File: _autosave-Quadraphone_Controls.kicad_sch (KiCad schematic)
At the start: 16 parts, among them SW1 SYNCH_SWITCH, SW2 DPDT_Switch

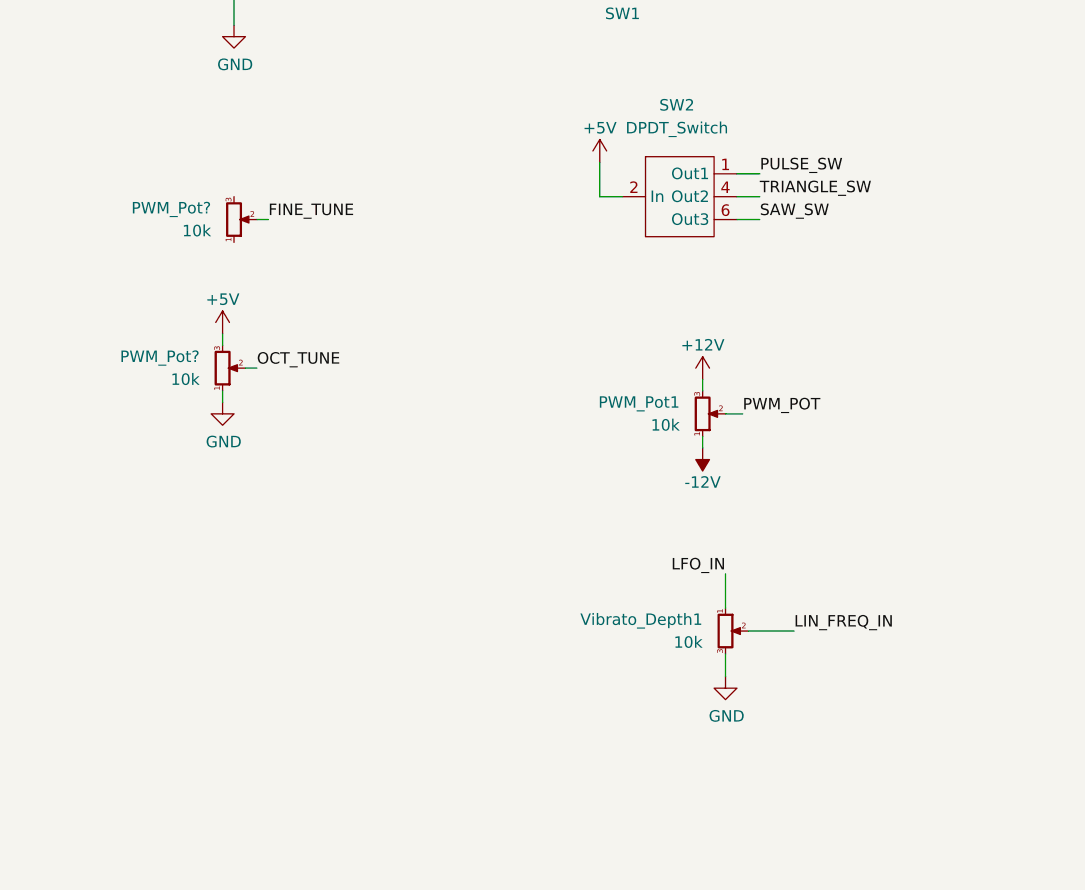
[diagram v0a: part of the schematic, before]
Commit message: Started control board schematic
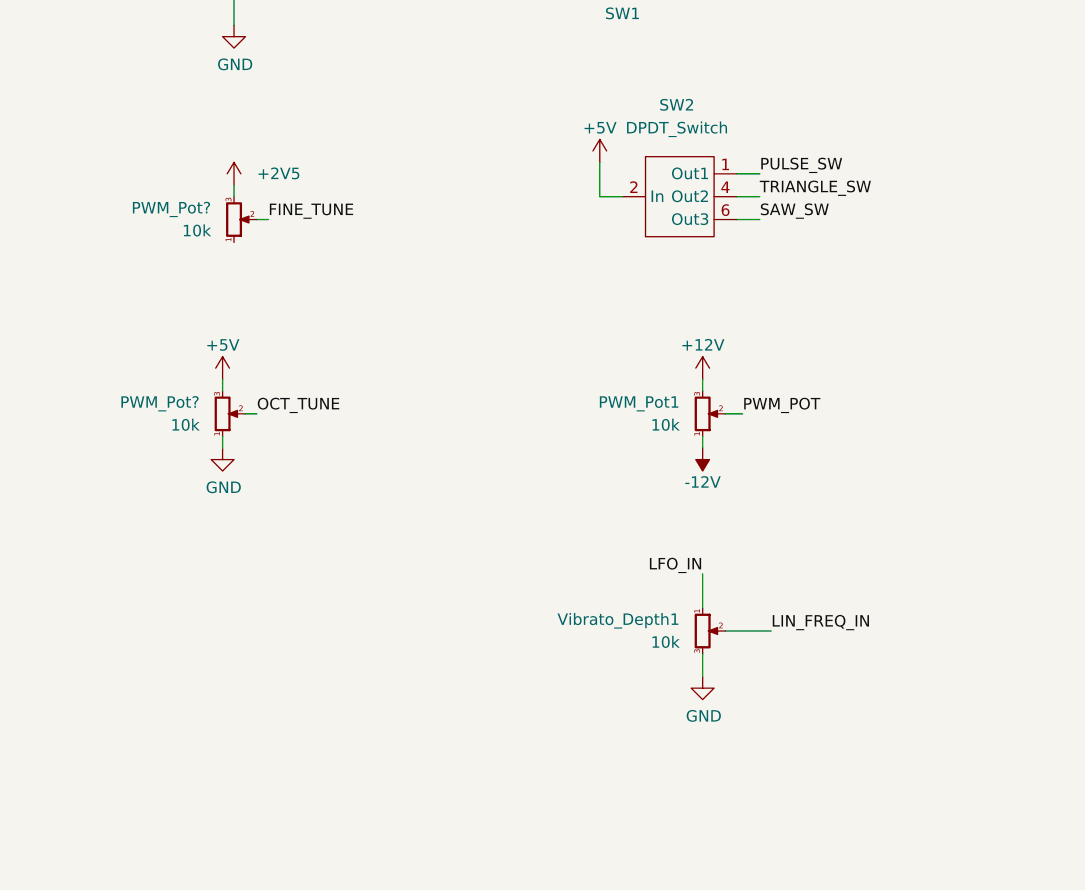
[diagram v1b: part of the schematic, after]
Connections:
- net +2V5: now also PWM_Pot?.3
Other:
- moved on the sheet: PWM_Pot?, Vibrato_Depth1
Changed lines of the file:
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@@
     (stroke (width 0) (type default) (color 0 0 0 0))
   )
-  (wire (pts (xy 36.83 95.25) (xy 36.83 93.98))
+  (wire (pts (xy 36.83 100.33) (xy 36.83 99.06))
     (stroke (width 0) (type default) (color 0 0 0 0))
   )
@@
     (stroke (width 0) (type default) (color 0 0 0 0))
   )
-  (wire (pts (xy 36.83 87.63) (xy 36.83 88.9))
-    (stroke (width 0) (type default) (color 0 0 0 0))
-  )
-  (wire (pts (xy 92.71 123.19) (xy 92.71 125.73))
+  (wire (pts (xy 36.83 92.71) (xy 36.83 93.98))
+    (stroke (width 0) (type default) (color 0 0 0 0))
+  )
+  (wire (pts (xy 90.17 123.19) (xy 90.17 125.73))
     (stroke (width 0) (type default) (color 0 0 0 0))
   )
@@
     (stroke (width 0) (type default) (color 0 0 0 0))
   )
-  (wire (pts (xy 95.25 120.65) (xy 100.33 120.65))
+  (wire (pts (xy 92.71 120.65) (xy 97.79 120.65))
     (stroke (width 0) (type default) (color 0 0 0 0))
   )
@@
     (stroke (width 0) (type default) (color 0 0 0 0))
   )
-  (wire (pts (xy 39.37 91.44) (xy 40.64 91.44))
+  (wire (pts (xy 39.37 96.52) (xy 40.64 96.52))
     (stroke (width 0) (type default) (color 0 0 0 0))
   )
@@
     (stroke (width 0) (type default) (color 0 0 0 0))
   )
-  (wire (pts (xy 92.71 114.3) (xy 92.71 118.11))
+  (wire (pts (xy 90.17 114.3) (xy 90.17 118.11))
     (stroke (width 0) (type default) (color 0 0 0 0))
   )
@@
     (stroke (width 0) (type default) (color 0 0 0 0))
   )
+  (wire (pts (xy 38.1 71.12) (xy 38.1 72.39))
+    (stroke (width 0) (type default) (color 0 0 0 0))
+  )
   (wire (pts (xy 74.93 46.99) (xy 77.47 46.99))
     (stroke (width 0) (type default) (color 0 0 0 0))
@@
     (effects (font (size 1.27 1.27)) (justify left bottom))
   )
-  (label "LFO_IN" (at 92.71 114.3 180)
+  (label "LFO_IN" (at 90.17 114.3 180)
     (effects (font (size 1.27 1.27)) (justify right bottom))
   )
@@
     (effects (font (size 1.27 1.27)) (justify left bottom))
   )
-  (label "LIN_FREQ_IN" (at 100.33 120.65 0)
+  (label "LIN_FREQ_IN" (at 97.79 120.65 0)
     (effects (font (size 1.27 1.27)) (justify left bottom))
   )
@@
     (effects (font (size 1.27 1.27)) (justify left bottom))
   )
-  (label "OCT_TUNE" (at 40.64 91.44 0)
+  (label "OCT_TUNE" (at 40.64 96.52 0)
     (effects (font (size 1.27 1.27)) (justify left bottom))
   )
@@
     (pin "1")
   )
-  (symbol (lib_id "Device:R_Potentiometer_Small") (at 36.83 91.44 0) (mirror x) (unit 1)
-    (in_bom yes) (on_board yes) (fields_autoplaced)
-    (property "Reference" "PWM_Pot?" (id 0) (at 34.29 90.1699 0)
-      (effects (font (size 1.27 1.27)) (justify right))
-    )
-    (property "Value" "10k" (id 1) (at 34.29 92.7099 0)
-      (effects (font (size 1.27 1.27)) (justify right))
-    )
-    (property "Footprint" "Custom_Footprints:Alpha_9mm_Potentiometer_Aligned" (id 2) (at 36.83 91.44 0)
-      (effects (font (size 1.27 1.27)) hide)
-    )
-    (property "Datasheet" "~" (id 3) (at 36.83 91.44 0)
+  (symbol (lib_id "Device:R_Potentiometer_Small") (at 36.83 96.52 0) (mirror x) (unit 1)
+    (in_bom yes) (on_board yes) (fields_autoplaced)
+    (property "Reference" "PWM_Pot?" (id 0) (at 34.29 95.2499 0)
+      (effects (font (size 1.27 1.27)) (justify right))
+    )
+    (property "Value" "10k" (id 1) (at 34.29 97.7899 0)
+      (effects (font (size 1.27 1.27)) (justify right))
+    )
+    (property "Footprint" "Custom_Footprints:Alpha_9mm_Potentiometer_Aligned" (id 2) (at 36.83 96.52 0)
+      (effects (font (size 1.27 1.27)) hide)
+    )
+    (property "Datasheet" "~" (id 3) (at 36.83 96.52 0)
       (effects (font (size 1.27 1.27)) hide)
     )
@@
     (pin "8")
   )
-  (symbol (lib_id "Device:R_Potentiometer_Small") (at 92.71 120.65 0) (unit 1)
-    (in_bom yes) (on_board yes) (fields_autoplaced)
-    (property "Reference" "Vibrato_Depth1" (id 0) (at 90.17 119.3799 0)
-      (effects (font (size 1.27 1.27)) (justify right))
-    )
-    (property "Value" "10k" (id 1) (at 90.17 121.9199 0)
-      (effects (font (size 1.27 1.27)) (justify right))
-    )
-    (property "Footprint" "Custom_Footprints:Alpha_9mm_Potentiometer_Aligned" (id 2) (at 92.71 120.65 0)
-      (effects (font (size 1.27 1.27)) hide)
-    )
-    (property "Datasheet" "~" (id 3) (at 92.71 120.65 0)
+  (symbol (lib_id "Device:R_Potentiometer_Small") (at 90.17 120.65 0) (unit 1)
+    (in_bom yes) (on_board yes) (fields_autoplaced)
+    (property "Reference" "Vibrato_Depth1" (id 0) (at 87.63 119.3799 0)
+      (effects (font (size 1.27 1.27)) (justify right))
+    )
+    (property "Value" "10k" (id 1) (at 87.63 121.9199 0)
+      (effects (font (size 1.27 1.27)) (justify right))
+    )
+    (property "Footprint" "Custom_Footprints:Alpha_9mm_Potentiometer_Aligned" (id 2) (at 90.17 120.65 0)
+      (effects (font (size 1.27 1.27)) hide)
+    )
+    (property "Datasheet" "~" (id 3) (at 90.17 120.65 0)
       (effects (font (size 1.27 1.27)) hide)
     )
@@
     (pin "1")
   )
-  (symbol (lib_id "power:GND") (at 36.83 95.25 0) (unit 1)
-    (in_bom yes) (on_board yes)
-    (property "Reference" "#PWR?" (id 0) (at 36.83 101.6 0)
-      (effects (font (size 1.27 1.27)) hide)
-    )
-    (property "Value" "GND" (id 1) (at 36.957 99.6442 0))
-    (property "Footprint" "" (id 2) (at 36.83 95.25 0)
-      (effects (font (size 1.27 1.27)) hide)
-    )
-    (property "Datasheet" "" (id 3) (at 36.83 95.25 0)
+  (symbol (lib_id "power:GND") (at 36.83 100.33 0) (unit 1)
+    (in_bom yes) (on_board yes)
+    (property "Reference" "#PWR?" (id 0) (at 36.83 106.68 0)
+      (effects (font (size 1.27 1.27)) hide)
+    )
+    (property "Value" "GND" (id 1) (at 36.957 104.7242 0))
+    (property "Footprint" "" (id 2) (at 36.83 100.33 0)
+      (effects (font (size 1.27 1.27)) hide)
+    )
+    (property "Datasheet" "" (id 3) (at 36.83 100.33 0)
       (effects (font (size 1.27 1.27)) hide)
     )
@@
     (pin "9")
   )
-  (symbol (lib_id "power:GND") (at 92.71 125.73 0) (unit 1)
-    (in_bom yes) (on_board yes)
-    (property "Reference" "#PWR023" (id 0) (at 92.71 132.08 0)
-      (effects (font (size 1.27 1.27)) hide)
-    )
-    (property "Value" "GND" (id 1) (at 92.837 130.1242 0))
-    (property "Footprint" "" (id 2) (at 92.71 125.73 0)
-      (effects (font (size 1.27 1.27)) hide)
-    )
-    (property "Datasheet" "" (id 3) (at 92.71 125.73 0)
-      (effects (font (size 1.27 1.27)) hide)
-    )
-    (pin "1")
-  )
-  (symbol (lib_id "power:+5V") (at 36.83 87.63 0) (unit 1)
-    (in_bom yes) (on_board yes)
-    (property "Reference" "#PWR?" (id 0) (at 36.83 91.44 0)
-      (effects (font (size 1.27 1.27)) hide)
-    )
-    (property "Value" "+5V" (id 1) (at 36.83 83.82 0))
-    (property "Footprint" "" (id 2) (at 36.83 87.63 0)
-      (effects (font (size 1.27 1.27)) hide)
-    )
-    (property "Datasheet" "" (id 3) (at 36.83 87.63 0)
+  (symbol (lib_id "power:GND") (at 90.17 125.73 0) (unit 1)
+    (in_bom yes) (on_board yes)
+    (property "Reference" "#PWR023" (id 0) (at 90.17 132.08 0)
+      (effects (font (size 1.27 1.27)) hide)
+    )
+    (property "Value" "GND" (id 1) (at 90.297 130.1242 0))
+    (property "Footprint" "" (id 2) (at 90.17 125.73 0)
+      (effects (font (size 1.27 1.27)) hide)
+    )
+    (property "Datasheet" "" (id 3) (at 90.17 125.73 0)
+      (effects (font (size 1.27 1.27)) hide)
+    )
+    (pin "1")
+  )
+  (symbol (lib_id "power:+5V") (at 36.83 92.71 0) (unit 1)
+    (in_bom yes) (on_board yes)
+    (property "Reference" "#PWR?" (id 0) (at 36.83 96.52 0)
+      (effects (font (size 1.27 1.27)) hide)
+    )
+    (property "Value" "+5V" (id 1) (at 36.83 88.9 0))
+    (property "Footprint" "" (id 2) (at 36.83 92.71 0)
+      (effects (font (size 1.27 1.27)) hide)
+    )
+    (property "Datasheet" "" (id 3) (at 36.83 92.71 0)
       (effects (font (size 1.27 1.27)) hide)
     )
@@
     (pin "3")
   )
+  (symbol (lib_id "power:+2V5") (at 38.1 71.12 0) (unit 1)
+    (in_bom yes) (on_board yes) (fields_autoplaced)
+    (property "Reference" "#PWR?" (id 0) (at 38.1 74.93 0)
+      (effects (font (size 1.27 1.27)) hide)
+    )
+    (property "Value" "+2V5" (id 1) (at 40.64 69.8499 0)
+      (effects (font (size 1.27 1.27)) (justify left))
+    )
+    (property "Footprint" "" (id 2) (at 38.1 71.12 0)
+      (effects (font (size 1.27 1.27)) hide)
+    )
+    (property "Datasheet" "" (id 3) (at 38.1 71.12 0)
+      (effects (font (size 1.27 1.27)) hide)
+    )
+    (pin "1")
+  )
   (symbol (lib_id "power:GND") (at 226.06 160.02 90) (unit 1)
     (in_bom yes) (on_board yes) (fields_autoplaced)
@@
       (reference "#PWR?") (unit 1) (value "+5V") (footprint "")
     )
+    (path "/f01cb584-8a0d-4eef-b1a6-375efa682fa6"
+      (reference "#PWR?") (unit 1) (value "+2V5") (footprint "")
+    )
     (path "/f141c9b1-c6fd-486d-92ca-316a0d17f43c"
